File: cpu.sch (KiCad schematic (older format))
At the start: 8 parts, among them SW5 NMI, U15 Z80CPU, U16 GAL16V8, U17 GAL16V8

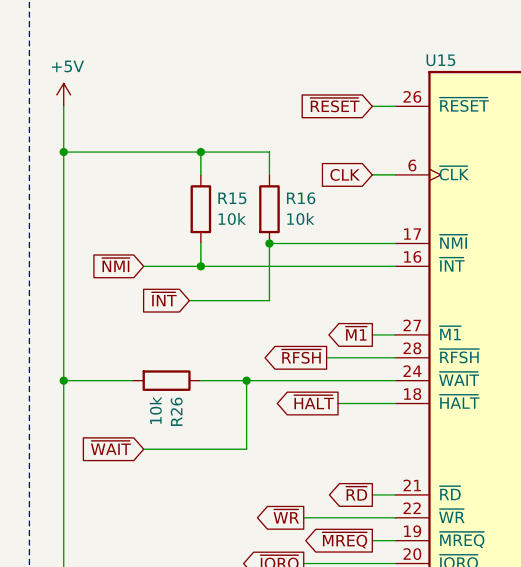
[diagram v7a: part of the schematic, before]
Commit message: Revision 2 bug fix. NMI / INT reversed. Added resistors to UART Rx/Tx
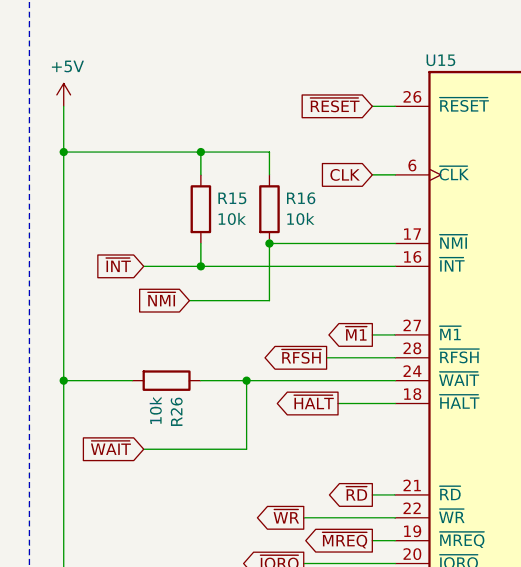
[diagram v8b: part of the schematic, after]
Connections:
- net ~INT: now also R15.2, U15.16 (~INT~); no longer R16.2, U15.17 (~NMI~)
- net ~NMI: now also R16.2, U15.17 (~NMI~); no longer R15.2, U15.16 (~INT~)
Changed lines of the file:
@@
 Wire Wire Line
 	1900 1950 1900 1850
-Wire Wire Line
-	1900 2250 1900 2500
-Connection ~ 1900 2250
 $Comp
 L power:+5V #PWR?
@@
 Wire Wire Line
 	8750 4200 8850 4200
-Connection ~ 1600 2350
 Wire Wire Line
 	1600 2350 2450 2350
@@
 Wire Wire Line
 	1900 2500 1550 2500
-Text GLabel 1550 2500 0    50   Input ~ 0
+Text GLabel 1350 2350 0    50   Input ~ 0
 ~INT
 Wire Wire Line
@@
 	1    0    0    -1
 $EndComp
-Wire Wire Line
-	1350 2350 1600 2350
-Text GLabel 1350 2350 0    50   Input ~ 0
-~NMI
 Text GLabel 1350 3150 0    50   Input ~ 0
 ~WAIT
@@
 Text Notes 1000 1050 0    47   ~ 0
 CPU
+Text GLabel 1550 2500 0    50   Input ~ 0
+~NMI
+Connection ~ 1600 2350
+Wire Wire Line
+	1350 2350 1600 2350
+Connection ~ 1900 2250
+Wire Wire Line
+	1900 2250 1900 2500
 Wire Bus Line
 	4250 3200 4250 3950
